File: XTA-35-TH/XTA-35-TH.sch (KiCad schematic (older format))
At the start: 30 parts, among them J1 XTA_Connector, J2 IBM_8bit_DBA, J3 XTA Power, J4 LED, J5 Debug, SW1 Config, SW2 Boot Internal, SW3 Reset, U1 74LVC245, U2 74LVC245, U3 74HCT125, U4 RPI_PICO, U5 74HC165

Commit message: More board work.
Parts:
- removed D2: MBR120/130, Diode_SMD:D_SOD-123, symbol Device:D_Schottky
- removed J2: IBM_8bit_DBA, symbol 00Custom:IBM_8bit_DBA
- removed R4, R5, R6: 10K, Resistor_SMD:R_1206_3216Metric, symbol Device:R
- J4: footprint (none) -> Connector_PinHeader_2.54mm:PinHeader_1x02_P2.54mm_Horizontal
- J5: footprint (none) -> Connector_PinHeader_2.54mm:PinHeader_1x06_P2.54mm_Vertical
- SW1: footprint (none) -> 00Common:SW_DIP_SPSTx04
- SW2, SW3: footprint (none) -> Button_Switch_THT:SW_PUSH_6mm
- U1, U2: footprint (none) -> Package_DIP:DIP-20_W7.62mm_Socket
- U3: footprint (none) -> Package_DIP:DIP-14_W7.62mm_Socket
- U5: footprint (none) -> Package_DIP:DIP-16_W7.62mm_Socket
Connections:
- net labels added: IRQ_SELECT, RESERVED, SD1_CS
- net labels removed: DRIVE_SIZE_0, DRIVE_SIZE_3, IBM_SENSE_12V, IBM_SENSE_3V3
- wire segments 216 -> 165
- no-connect marks 13 -> 6
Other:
- moved on the sheet: R10, R11, R7, R8, R9, SW1, SW2, U5

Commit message: Lots of board layout.
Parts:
- added J2: SD0, 00Common:SD_Board, symbol Connector_Generic:Conn_01x06
- added J6: SD1, 00Common:SD_Board, symbol Connector_Generic:Conn_01x06
- added MH1, MH2, MH3, MH4: MountingHole_Pad, 00Common:Reinforcing_Ring_Partial, symbol Mechanical:MountingHole_Pad
- added R4: 10K, Resistor_SMD:R_1206_3216Metric, symbol Device:R
- U2: symbol 74xx:74LS245 -> 00Custom:74LS245_One_Way
- renumbered R7 to R5, R8 to R6, R9 to R7, R10 to R8, R11 to R9, U5 to U4, U4 to U5
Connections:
- net SD1_CS is gone; now on net CFG_LATCH: U5.34 (GP28)
- net +3V3: now also C4.1, J2.1 (Pin_1), J6.1 (Pin_1); no longer C3.1
- net +5V: now also C3.1, R4.2; no longer C4.1, U3.12, U3.9
- net A0_3V3: now also U5.19 (GP14); no longer U5.14 (GP10)
- net A1_3V3: now also U5.20 (GP15); no longer U5.15 (GP11)
- net AEN_3V3: now also U5.7 (GP5); no longer U5.16 (GP12)
- net BOOT_INTERNAL: now also U4.11 (D0); no longer U4.3 (D4)
- net CFG_LATCH: now also J6.2 (Pin_2)
- net D0_3V3: now also U5.9 (GP6); no longer U5.4 (GP2)
- net D1_3V3: now also U5.10 (GP7); no longer U5.5 (GP3)
- net D2_3V3: now also U5.11 (GP8); no longer U5.6 (GP4)
- net D3_3V3: now also U5.12 (GP9); no longer U5.7 (GP5)
- net D4_3V3: now also U5.14 (GP10); no longer U5.9 (GP6)
- net D5_3V3: now also U5.15 (GP11); no longer U5.10 (GP7)
- net D6_3V3: now also U5.16 (GP12); no longer U5.11 (GP8)
- net D7_3V3: now also U5.17 (GP13); no longer U5.12 (GP9)
- net DRIVE_SIZE_2: now also SW1.3, U4.5 (D6); no longer SW1.6, U4.13 (D2)
- net GND: now also J5.2 (Pin_2), J5.5 (Pin_5), U4.12 (D1), U4.13 (D2), U4.14 (D3), U5.42 (GND), J2.6 (Pin_6), J6.6 (Pin_6); no longer U4.4 (D5), U4.5 (D6), U4.6 (D7)
- net IRQ_SELECT: now also SW1.2, U4.4 (D5); no longer SW1.7, U4.12 (D1)
- net RESERVED: now also SW1.4, U4.6 (D7); no longer SW1.5, U4.14 (D3)
- net RESET_INVERT: now also SW1.1, U4.3 (D4); no longer SW1.8, U4.11 (D0)
- net SD0_CS: now also J2.2 (Pin_2)
- net SD_DI: now also J2.5 (Pin_5), J6.5 (Pin_5)
- net SD_DO: now also J2.3 (Pin_3), J6.3 (Pin_3)
- net SD_SCK: now also J2.4 (Pin_4), J6.4 (Pin_4)
- net ~DACK~_3V3: now also U5.6 (GP4); no longer U5.17 (GP13)
- net ~DRQ~_3V3: now also U5.5 (GP3); no longer U5.19 (GP14)
- net ~IRQ~_3V3: now also U5.4 (GP2); no longer U5.20 (GP15)
- net at R5.1: now also SW1.6; no longer SW1.1
- net at R6.1: now also SW1.7; no longer SW1.2
- net at R7.1: now also SW1.8; no longer SW1.3
- net at R8.1: now also SW1.5; no longer SW1.4
- net IBM_5V_POWER: no longer names the net of D1.2 (A), J3.4 (Pin_4)
- new net: R4.1, U3.12, U3.9
- new net MOUNTING_1: MH1.1
- new net MOUNTING_2: MH2.1
- new net MOUNTING_3: MH3.1
- new net MOUNTING_4: MH4.1
- no-connect marks 6 -> 10
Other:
- note added: "IDE CONNECTOR"
- note added: "SD CONNECTORS"
- note removed: "INTERFACE CONNECTORS"
- moved on the sheet: C1, C2, C3, C4, D1, J1, R5, R6, R7, R8, R9, SW1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

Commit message: Board layout WIP.
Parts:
- added MH5, MH6, MH7, MH8: MountingHole_Pad, MountingHole:MountingHole_3.2mm_M3_Pad, symbol Mechanical:MountingHole
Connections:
- net CFG_CLK: now also U3.10; no longer R3.1, U3.4
- net CFG_LATCH: now also J2.2 (Pin_2), U5.4 (GP2); no longer J6.2 (Pin_2), U5.34 (GP28)
- net DBG_RX: now also R3.1
- net DRQ: now also U3.11; no longer U3.8
- net GND: now also U3.9; no longer U3.5
- net IRQ: now also U3.6; no longer U3.11
- net ~CS~_3V3: now also U5.22 (GP17); no longer U5.32 (GP27)
- net ~DRIVE_ACTIVE: now also U3.8; no longer U3.3
- net ~DRQ~_3V3: now also U3.13, U5.27 (GP21); no longer U3.10, U5.5 (GP3)
- net ~IOR~_3V3: now also U5.32 (GP27); no longer U5.26 (GP20)
- net ~IOW~_3V3: now also U5.34 (GP28); no longer U5.27 (GP21)
- net ~IRQ~_3V3: now also U3.4, U5.26 (GP20); no longer U3.13, U5.4 (GP2)
- net at R4.1, U3.12: now also U3.5; no longer U3.9
- net at R1.2: now also U3.3; no longer U3.6
- removed net SD0_CS: J2.2 (Pin_2), U5.22 (GP17)
- new net SD1_CS: J6.2 (Pin_2), U5.5 (GP3)
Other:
- note added: "MOUNTING"
- moved on the sheet: J2, J6, MH1, MH2, MH3, MH4, R5, R6, R7, R8, R9, SW1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

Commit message: Lots of board layout work.
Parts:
- renumbered R8 to R5, R5 to R8
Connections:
- net +3V3: now also R5.1, R6.1, R7.1, R8.1, R9.1; no longer R5.2, R6.2, R7.2, R8.2, R9.2
- net A0_3V3: now also U5.16 (GP12); no longer U5.19 (GP14)
- net A1_3V3: now also U5.17 (GP13); no longer U5.20 (GP15)
- net AEN_3V3: now also U5.19 (GP14); no longer U5.7 (GP5)
- net BOOT_INTERNAL: now also R9.2; no longer R9.1
- net CFG_CLK: now also U3.13; no longer U3.1
- net D0_3V3: now also U5.6 (GP4); no longer U5.9 (GP6)
- net D1_3V3: now also U5.7 (GP5); no longer U5.10 (GP7)
- net D2_3V3: now also U5.9 (GP6); no longer U5.11 (GP8)
- net D3_3V3: now also U5.10 (GP7); no longer U5.12 (GP9)
- net D4_3V3: now also U5.11 (GP8); no longer U5.14 (GP10)
- net D5_3V3: now also U5.12 (GP9); no longer U5.15 (GP11)
- net D6_3V3: now also U5.14 (GP10); no longer U5.16 (GP12)
- net D7_3V3: now also U5.15 (GP11); no longer U5.17 (GP13)
- net DRQ: now also U3.3; no longer U3.11
- net GND: now also SW1.5, SW1.6, SW1.7, SW1.8, U3.12; no longer U3.2
- net IRQ_SELECT: now also R5.2, SW1.1, U4.3 (D4); no longer SW1.2, U4.4 (D5)
- net RESET_INVERT: now also R8.2, SW1.2, U4.4 (D5); no longer SW1.1, U4.3 (D4)
- net ~CS~_3V3: now also U5.31 (GP26); no longer U5.22 (GP17)
- net ~DACK~_3V3: now also U5.20 (GP15); no longer U5.6 (GP4)
- net ~DRQ~_3V3: now also U3.1, U5.34 (GP28); no longer U3.13, U5.27 (GP21)
- net ~IOR~_3V3: now also U5.22 (GP17); no longer U5.32 (GP27)
- net ~IOW~_3V3: now also U5.26 (GP20); no longer U5.34 (GP28)
- net ~IRQ~_3V3: now also U5.32 (GP27); no longer U5.26 (GP20)
- net ~RESET~_3V3: now also U5.27 (GP21); no longer U5.31 (GP26)
- net ADC_VREF: now reaches U5.35 (ADC_VREF)
- net 3V3_EN: now reaches U5.37 (3V3_EN)
- net 5V_IN: now reaches D1.2 (A), J3.4 (Pin_4)
- net at R4.1, U3.5: now also U3.2; no longer U3.12
- net at R1.2: now also U3.11; no longer U3.3
- net DRIVE_SIZE_2 renamed OPTION_3
- net OPTION_3: now also R6.2
- net RESERVED renamed OPTION_4
- net OPTION_4: now also R7.2
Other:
- moved on the sheet: D1, R5, R6, R7, R8, R9, SW1, SW2, U3A, U3D

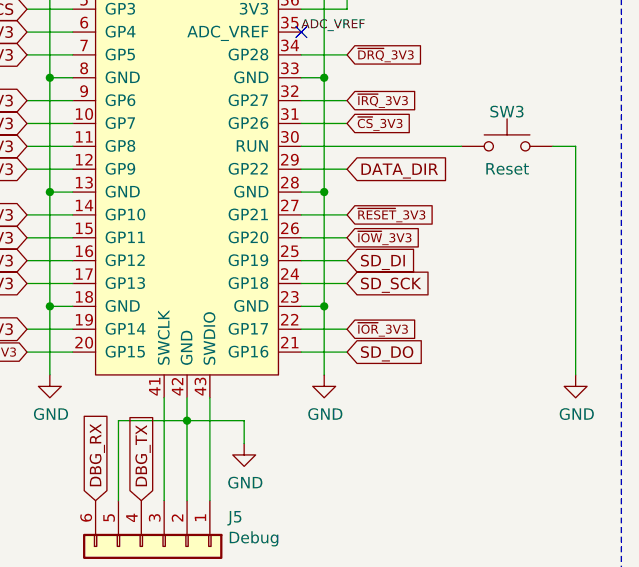
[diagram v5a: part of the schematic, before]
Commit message: Finished first pass on copper layers.
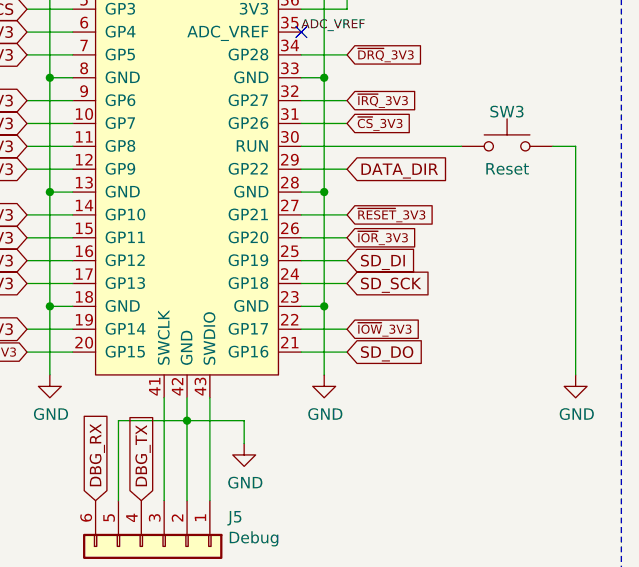
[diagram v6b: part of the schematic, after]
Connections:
- net ~IOR~_3V3: now also U5.26 (GP20); no longer U5.22 (GP17)
- net ~IOW~_3V3: now also U5.22 (GP17); no longer U5.26 (GP20)
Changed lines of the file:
@@
 Text GLabel 9900 4350 2    39   Input ~ 0
 ~IRQ~_3V3
+Text GLabel 9900 4950 2    39   Input ~ 0
+~IOR~_3V3
 Text GLabel 9900 5350 2    39   Input ~ 0
-~IOR~_3V3
-Text GLabel 9900 4950 2    39   Input ~ 0
 ~IOW~_3V3
 Text GLabel 9900 4850 2    39   Input ~ 0

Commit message: Finished first pass of board design.
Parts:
- J1: footprint Connector_PinHeader_2.54mm:PinHeader_2x20_P2.54mm_Horizontal -> Connector_IDC:IDC-Header_2x20_P2.54mm_Horizontal
- J4: renamed from J2; symbol Connector_Generic:Conn_01x06 -> 00Custom:SD_Board
- J5: renamed from J6; symbol Connector_Generic:Conn_01x06 -> 00Custom:SD_Board
- U5: value RPI_PICO -> Raspberry Pi Pico
- renumbered J3 to J2, J4 to J3, J5 to J6
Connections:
- net SWCLK: now reaches J6.3 (Pin_3), U5.41 (SWCLK)
- net SWDIO: now reaches J6.1 (Pin_1), U5.43 (SWDIO)
- net SD_DI renamed SPI_RX
- net SPI_RX: now also U5.21 (GP16); no longer U5.25 (GP19)
- net SD_DO renamed SPI_TX
- net SPI_TX: now also U5.25 (GP19); no longer U5.21 (GP16)
- net SD_SCK renamed SPI_SCK
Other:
- moved on the sheet: J4, J5
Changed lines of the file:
@@
 F 0 "J1" H 1750 3165 50  0000 C CNN
 F 1 "XTA_Connector" H 1750 3074 50  0000 C CNN
-F 2 "Connector_PinHeader_2.54mm:PinHeader_2x20_P2.54mm_Horizontal" H 1750 3050 50  0001 C CNN
+F 2 "Connector_IDC:IDC-Header_2x20_P2.54mm_Horizontal" H 1750 3050 50  0001 C CNN
 F 3 "" H 1750 3050 50  0001 C CNN
 	1    1750 2000
@@
 P 9200 4450
 F 0 "U5" H 9200 5615 50  0000 C CNN
-F 1 "RPI_PICO" H 9200 5524 50  0000 C CNN
+F 1 "Raspberry Pi Pico" H 9200 5524 50  0000 C CNN
 F 2 "Pico:RPi_Pico_SMD_TH" H 9200 5450 50  0001 C CNN
 F 3 "" H 9200 5450 50  0001 C CNN
@@
 $EndComp
 $Comp
-L Connector_Generic:Conn_01x02 J4
+L Connector_Generic:Conn_01x02 J3
 U 1 1 61901414
 P 7150 5300
-F 0 "J4" H 7230 5292 50  0000 L CNN
+F 0 "J3" H 7230 5292 50  0000 L CNN
 F 1 "LED" H 7230 5201 50  0000 L CNN
 F 2 "Connector_PinHeader_2.54mm:PinHeader_1x02_P2.54mm_Horizontal" H 7150 5300 50  0001 C CNN
@@
 	6250 5750 6250 5650
 Text GLabel 9900 5450 2    50   Input ~ 0
-SD_DO
+SPI_RX
 Text GLabel 9900 5050 2    50   Input ~ 0
-SD_DI
+SPI_TX
 Text GLabel 9900 5150 2    50   Input ~ 0
-SD_SCK
-$Comp
-L Connector_Generic:Conn_01x06 J5
+SPI_SCK
+$Comp
+L Connector_Generic:Conn_01x06 J6
 U 1 1 61700DAF
 P 9100 6300
-F 0 "J5" V 8972 6580 50  0000 L CNN
+F 0 "J6" V 8972 6580 50  0000 L CNN
 F 1 "Debug" V 9063 6580 50  0000 L CNN
 F 2 "Connector_PinHeader_2.54mm:PinHeader_1x06_P2.54mm_Vertical" H 9100 6300 50  0001 C CNN
@@
 	8600 3550 8700 3550
 $Comp
-L Connector_Generic:Conn_01x04 J3
+L Connector_Generic:Conn_01x04 J2
 U 1 1 618296A7
 P 850 7050
-F 0 "J3" H 768 7367 50  0000 C CNN
+F 0 "J2" H 768 7367 50  0000 C CNN
 F 1 "XTA Power" H 768 7276 50  0000 C CNN
 F 2 "w_conn_pc:conn_hdd_15-24-4441" H 850 7050 50  0001 C CNN
@@
 SD1_CS
 $Comp
-L Connector_Generic:Conn_01x06 J2
+L 00Custom:SD_Board J4
 U 1 1 61736542
 P 3450 1450
-F 0 "J2" V 3322 1730 50  0000 L CNN
-F 1 "SD0" V 3413 1730 50  0000 L CNN
+F 0 "J4" H 3450 1850 50  0000 L CNN
+F 1 "SD0" H 3450 1750 50  0000 L CNN
 F 2 "00Common:SD_Board" H 3450 1450 50  0001 C CNN
 F 3 "~" H 3450 1450 50  0001 C CNN
@@
 	3150 1250 3250 1250
 Text GLabel 3250 1450 0    50   Input ~ 0
-SD_DO
+SPI_TX
 Text GLabel 3250 1350 0    50   Input ~ 0
 SD0_CS
 Text GLabel 3250 1550 0    50   Input ~ 0
-SD_SCK
+SPI_SCK
 Text GLabel 3250 1650 0    50   Input ~ 0
-SD_DI
+SPI_RX
 $Comp
 L power:GND #PWR0103
@@
 	3150 1750 3150 1850
 $Comp
-L Connector_Generic:Conn_01x06 J6
+L 00Custom:SD_Board J5
 U 1 1 61749C73
 P 3450 2700
-F 0 "J6" V 3322 2980 50  0000 L CNN
-F 1 "SD1" V 3413 2980 50  0000 L CNN
+F 0 "J5" H 3450 3100 50  0000 L CNN
+F 1 "SD1" H 3450 3000 50  0000 L CNN
 F 2 "00Common:SD_Board" H 3450 2700 50  0001 C CNN
 F 3 "~" H 3450 2700 50  0001 C CNN
@@
 	3150 2500 3250 2500
 Text GLabel 3250 2700 0    50   Input ~ 0
-SD_DO
+SPI_TX
 Text GLabel 3250 2600 0    50   Input ~ 0
 SD1_CS
 Text GLabel 3250 2800 0    50   Input ~ 0
-SD_SCK
+SPI_SCK
 Text GLabel 3250 2900 0    50   Input ~ 0
-SD_DI
+SPI_RX
 $Comp
 L power:GND #PWR0105
@@
 L power:GND #PWR0106
 U 1 1 6175F5F5
-P 9450 5850
-F 0 "#PWR0106" H 9450 5600 50  0001 C CNN
-F 1 "GND" H 9455 5677 50  0000 C CNN
-F 2 "" H 9450 5850 50  0001 C CNN
-F 3 "" H 9450 5850 50  0001 C CNN
-	1    9450 5850
-	1    0    0    -1
-$EndComp
-Wire Wire Line
-	9200 5750 9450 5750
-Wire Wire Line
-	9450 5750 9450 5850
+P 9600 5850
+F 0 "#PWR0106" H 9600 5600 50  0001 C CNN
+F 1 "GND" H 9605 5677 50  0000 C CNN
+F 2 "" H 9600 5850 50  0001 C CNN
+F 3 "" H 9600 5850 50  0001 C CNN
+	1    9600 5850
+	1    0    0    -1
+$EndComp
+Wire Wire Line
+	9200 5750 9600 5750
+Wire Wire Line
+	9600 5750 9600 5850
 Text GLabel 8050 3950 0    50   Input ~ 0
 CFG_LATCH
@@
 Text Label 1200 7250 0    50   ~ 0
 5V_IN
+Text Label 9300 6100 1    30   ~ 0
+SWDIO
+Text Label 9100 6100 1    30   ~ 0
+SWCLK
 $EndSCHEMATC

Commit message: Production files. Also added a relief USB connector body after sending for production.
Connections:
- net BOOT_INTERNAL renamed BOOT_OVERRIDE
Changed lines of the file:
@@
 OPTION_4
 Text Label 8750 1250 0    50   ~ 0
-BOOT_INTERNAL
+BOOT_OVERRIDE
 $Comp
 L Switch:SW_DIP_x04 SW1
